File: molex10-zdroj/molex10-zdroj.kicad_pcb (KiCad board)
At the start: 2 copper layers, 52 x 52 mm, 9 parts, among them J1 Conn_01x04, J2 Conn_02x04_Counter_Clockwise, J3 Conn_01x04, J4 Conn_01x02, J5 Conn_01x02

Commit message: Use screw terminal symbols, use MVE25-5-V as values.
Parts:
- J1, J3: value Conn_01x04 -> MVE253-5-V
- J4, J5: value Conn_01x02 -> MVE252-5-V
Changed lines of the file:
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@@
     (property "Sheetfile" "molex10-zdroj.kicad_sch")
     (property "Sheetname" "")
-    (property "ki_description" "Generic connector, single row, 01x02, script generated (kicad-library-utils/schlib/autogen/connector/)")
-    (property "ki_keywords" "connector")
+    (property "ki_description" "Generic screw terminal, single row, 01x02, script generated (kicad-library-utils/schlib/autogen/connector/)")
+    (property "ki_keywords" "screw terminal")
     (attr through_hole)
     (fp_text reference "J4" (at -0.022 -6 unlocked) (layer "F.SilkS") hide
         (effects (font (size 1 1) (thickness 0.15)))
     )
-    (fp_text value "Conn_01x02" (at -0.122 5.8 unlocked) (layer "F.Fab")
+    (fp_text value "MVE252-5-V" (at -0.122 5.8 unlocked) (layer "F.Fab")
         (effects (font (size 1 1) (thickness 0.15)))
     )
@@
     (property "Sheetfile" "molex10-zdroj.kicad_sch")
     (property "Sheetname" "")
-    (property "ki_description" "Generic connector, single row, 01x03, script generated (kicad-library-utils/schlib/autogen/connector/)")
-    (property "ki_keywords" "connector")
+    (property "ki_description" "Generic screw terminal, single row, 01x03, script generated (kicad-library-utils/schlib/autogen/connector/)")
+    (property "ki_keywords" "screw terminal")
     (attr through_hole)
     (fp_text reference "J1" (at 0 -6 unlocked) (layer "F.SilkS") hide
         (effects (font (size 1 1) (thickness 0.15)))
     )
-    (fp_text value "Conn_01x04" (at 0 5.75 unlocked) (layer "F.Fab")
+    (fp_text value "MVE253-5-V" (at 0 5.75 unlocked) (layer "F.Fab")
         (effects (font (size 1 1) (thickness 0.15)))
     )
@@
     (property "Sheetfile" "molex10-zdroj.kicad_sch")
     (property "Sheetname" "")
-    (property "ki_description" "Generic connector, single row, 01x03, script generated (kicad-library-utils/schlib/autogen/connector/)")
-    (property "ki_keywords" "connector")
+    (property "ki_description" "Generic screw terminal, single row, 01x03, script generated (kicad-library-utils/schlib/autogen/connector/)")
+    (property "ki_keywords" "screw terminal")
     (attr through_hole)
     (fp_text reference "J3" (at 0 -6 180 unlocked) (layer "F.SilkS") hide
         (effects (font (size 1 1) (thickness 0.15)))
     )
-    (fp_text value "Conn_01x04" (at 0 5.75 180 unlocked) (layer "F.Fab")
+    (fp_text value "MVE253-5-V" (at 0 5.75 180 unlocked) (layer "F.Fab")
         (effects (font (size 1 1) (thickness 0.15)))
     )
@@
     (property "Sheetfile" "molex10-zdroj.kicad_sch")
     (property "Sheetname" "")
-    (property "ki_description" "Generic connector, single row, 01x02, script generated (kicad-library-utils/schlib/autogen/connector/)")
-    (property "ki_keywords" "connector")
+    (property "ki_description" "Generic screw terminal, single row, 01x02, script generated (kicad-library-utils/schlib/autogen/connector/)")
+    (property "ki_keywords" "screw terminal")
     (attr through_hole)
     (fp_text reference "J5" (at -0.022 -6 180 unlocked) (layer "F.SilkS") hide
         (effects (font (size 1 1) (thickness 0.15)))
     )
-    (fp_text value "Conn_01x02" (at -0.122 5.8 180 unlocked) (layer "F.Fab")
-        (effects (font (size 1 1) (thickness 0.15)))
-    )
+    (fp_text value "MVE252-5-V" (at -0.122 5.8 180 unlocked) (layer "F.Fab")
+        (effects (font (size 1 1) (thickness 0.15)))
+    )

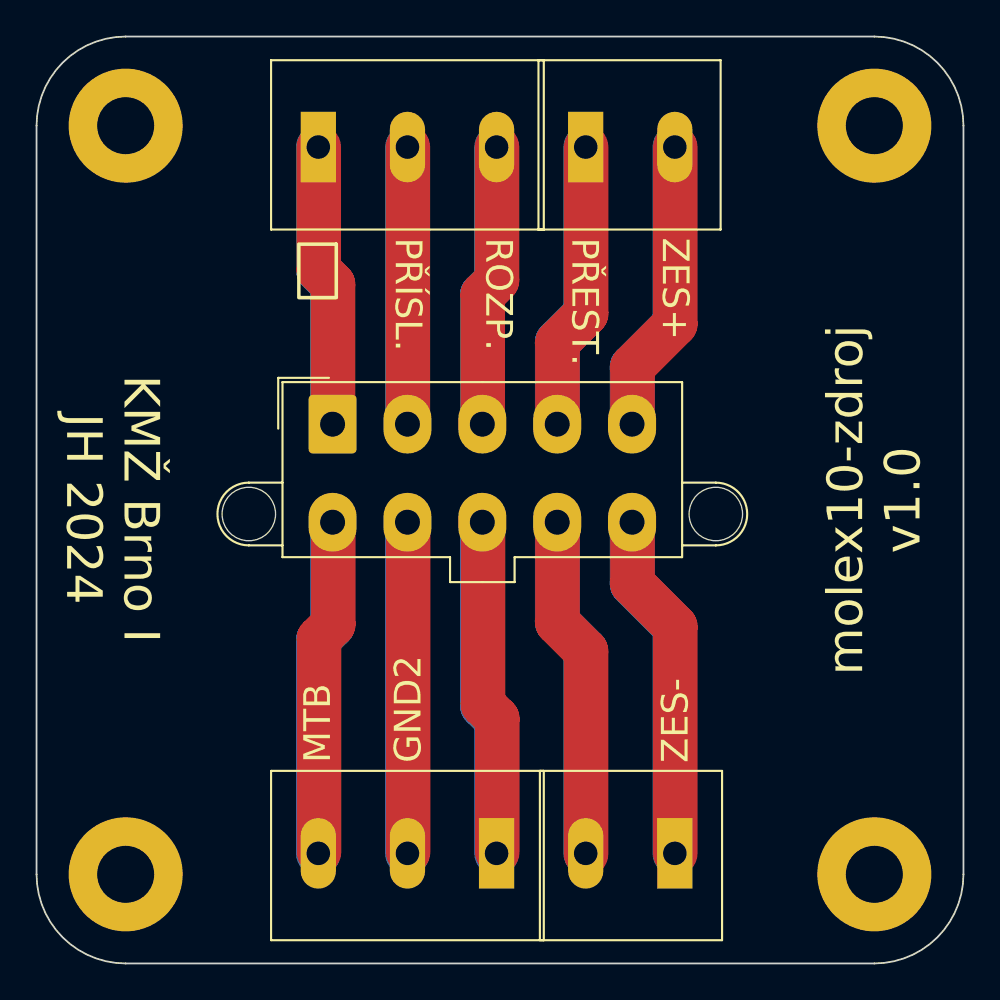
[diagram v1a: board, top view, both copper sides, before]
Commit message: molex10-zdroj: flip MOLEX to bottom side.
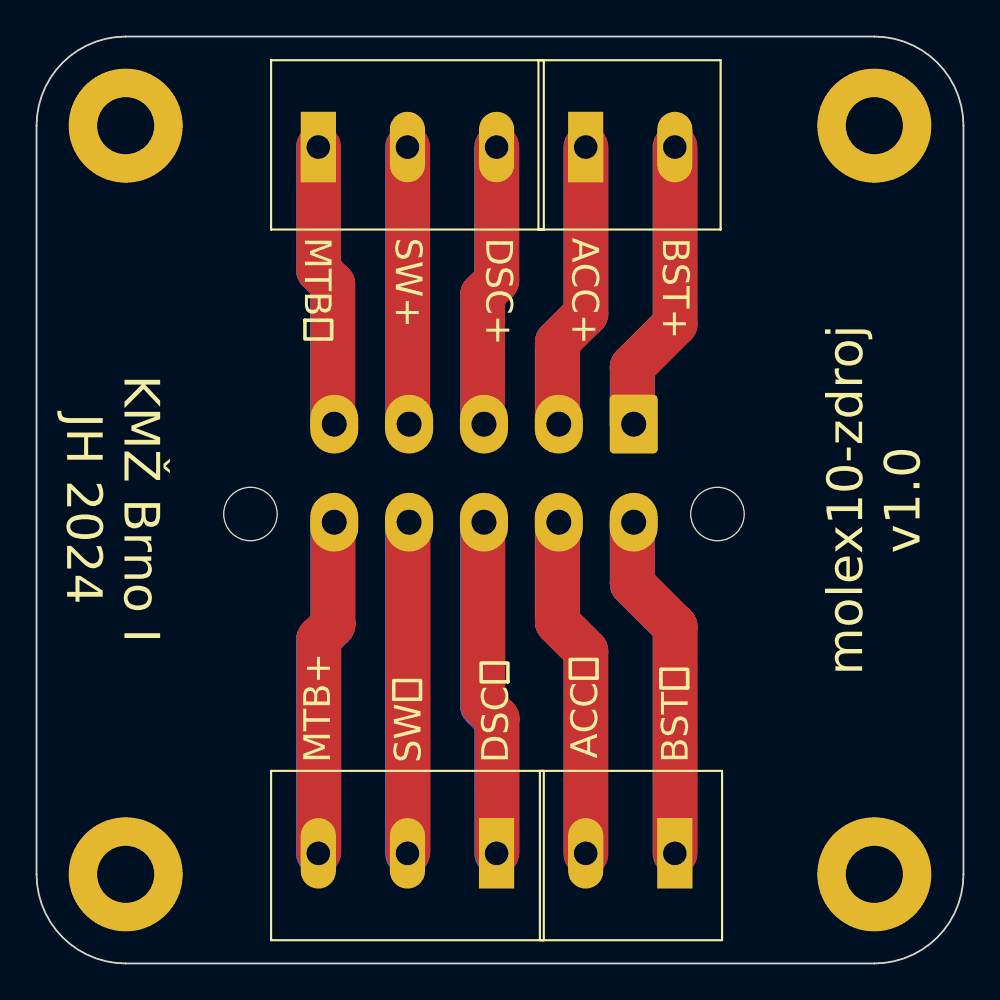
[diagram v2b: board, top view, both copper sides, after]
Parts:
- H1, H2, H3, H4: value MountingHole -> MountingHole-3.2mm
- J2: value Conn_02x04_Counter_Clockwise -> TME 39281103 MOLEX; moved to B.Cu
- moved J2 16.9 mm to (114.0, 91.7), turned to 180 degrees
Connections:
- net /DISC renamed /DSC
- net Net-(J2-Pin_8) renamed /GND-DSC
- J1 pad 1: /GND -> /BOOST+
- J1 pad 2: /ACC -> /SWITCH
- J2 pad 7: /GND2 -> /GND-ACC
- J2 pad 9: Net-(J2-Pin_9) -> /GND-SWITCH
- J3 pad 2: /GND2 -> /GND-SWITCH
- J3 pad 3: /MTB -> /BOOST-
- J4 pad 1: /SWITCH -> /ACC
- J4 pad 2: /BOOST+ -> /GND
- J5 pad 1: /BOOST- -> /MTB
- J5 pad 2: Net-(J2-Pin_9) -> /GND-ACC
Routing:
- net Net-(J2-Pin_9): track 38.5 -> 0.00 mm
- net /GND-ACC: track 0.00 -> 38.5 mm
- net /GND2: track 37.2 -> 0.00 mm
- net /GND-SWITCH: track 0.00 -> 37.2 mm
- net /SWITCH: track 32.4 -> 31.1 mm
- net /MTB: track 37.8 -> 39.1 mm
- net /BOOST-: track 39.1 -> 37.8 mm
- net /ACC: track 31.1 -> 32.4 mm
- net /GND: track 31.8 -> 33.1 mm
- net /BOOST+: track 33.1 -> 31.8 mm
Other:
- board text added: "ACC+"
- board text added: "ACC⏚"
- board text added: "BST+"
- board text added: "BST⏚"
- board text added: "DSC+"
- board text added: "DSC⏚"
- board text added: "MTB+"
- board text added: "MTB⏚"
- board text added: "SW+"
- board text added: "SW⏚"
- board text removed: "GND2"
- board text removed: "MTB"
- board text removed: "PŘEST."
- board text removed: "PŘÍSL."
- board text removed: "ROZP."
- board text removed: "ZES+"
- board text removed: "ZES-"
- board text removed: "⏚"
